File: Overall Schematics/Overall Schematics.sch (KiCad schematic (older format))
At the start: 31 parts, among them J1 WattMeter1_Output, J2 WattMeter2_Output, J3 Intel_Buck_Converter_Input, J4 WattMeter1_Input, J5 WattMeter2_Input, M1 Stepper_Motor_bipolar, M10 Motor_Servo, M11 Stepper_Motor_bipolar, M2 Stepper_Motor_bipolar, M3 LinActuator12V, M4 LinActuator12V, M5 LinActuator12V, M6 Motor_DC, M7 Motor_DC, M8 Motor_DC, M9 Motor_DC, SW1 SW_DPST, U1 Teensy4.1, U10 VNH52019, U11 ServoDriver, U12 36v4SMD, U2 36v4SMD, U3 36v4SMD, U4 VNH52019, U5 VNH52019, U6 VNH52019, U7 VNH52019, U8 VNH52019, U9 VNH52019

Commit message: did some pcb stuff
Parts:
- added M12: Motor_Servo, TerminalBlock:TerminalBlock_bornier-3_P5.08mm, symbol Motor:Motor_Servo
- BT1, BT2: footprint Custom Footprints:AMASS_XT60-F_1x02_P7.20mm_Vertical -> (none)
- J4, J5: footprint TerminalBlock:TerminalBlock_bornier-2_P5.08mm -> (none)
- SW1: footprint Button_Switch_SMD:SW_MEC_5GSH9 -> (none)
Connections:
- net Battery1_Positive24V: no longer J2.2 (Pin_2), U12.17 (VIN), U12.18 (VIN2), U2.17 (VIN), U2.18 (VIN2), U5.14 (VIN(5.5V-24V)), U7.14 (VIN(5.5V-24V)), U8.14 (VIN(5.5V-24V))
- net GND: now also M10.3 (-), U11.13 (-_1), U11.14 (-_2), M12.3 (-)
- net SS_1: now reaches M10.1 (PWM), U11.1 (Signal_1)
- net SS_2: now reaches U11.2 (Signal_2)
- net SS_2: now also M12.1 (PWM)
- net +5V: now reaches M10.2 (+), U11.7 (+_1)
- net +5V: now also U11.8 (+_2), M12.2 (+)
- net Battery1_Positive renamed Battery2_Positive
- new net Battery2_Positive24V: J2.2 (Pin_2), U12.17 (VIN), U12.18 (VIN2), U2.17 (VIN), U2.18 (VIN2), U5.14 (VIN(5.5V-24V)), U7.14 (VIN(5.5V-24V)), U8.14 (VIN(5.5V-24V))
- no-connect marks 103 -> 100
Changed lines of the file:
@@
 F 0 "BT1" V 27455 13850 50  0000 C CNN
 F 1 "True_Spec_Battery1" V 27546 13850 50  0000 C CNN
-F 2 "Custom Footprints:AMASS_XT60-F_1x02_P7.20mm_Vertical" V 27700 13910 50  0001 C CNN
+F 2 "" V 27700 13910 50  0001 C CNN
 F 3 "~" V 27700 13910 50  0001 C CNN
 	1    27700 13850
@@
 F 0 "SW1" H 28700 14475 50  0000 C CNN
 F 1 "SW_DPST" H 28700 14384 50  0000 C CNN
-F 2 "Button_Switch_SMD:SW_MEC_5GSH9" H 28700 14150 50  0001 C CNN
+F 2 "" H 28700 14150 50  0001 C CNN
 F 3 "~" H 28700 14150 50  0001 C CNN
 	1    28700 14150
@@
 F 0 "BT2" V 27455 14250 50  0000 C CNN
 F 1 "True_Spec_Battery2" V 27546 14250 50  0000 C CNN
-F 2 "Custom Footprints:AMASS_XT60-F_1x02_P7.20mm_Vertical" V 27700 14310 50  0001 C CNN
+F 2 "" V 27700 14310 50  0001 C CNN
 F 3 "~" V 27700 14310 50  0001 C CNN
 	1    27700 14250
@@
 F 0 "J4" H 29530 13842 50  0000 L CNN
 F 1 "WattMeter1_Input" H 29530 13751 50  0000 L CNN
-F 2 "TerminalBlock:TerminalBlock_bornier-2_P5.08mm" H 29450 13850 50  0001 C CNN
+F 2 "" H 29450 13850 50  0001 C CNN
 F 3 "~" H 29450 13850 50  0001 C CNN
 	1    29450 13850
@@
 F 0 "J5" H 29530 14292 50  0000 L CNN
 F 1 "WattMeter2_Input" H 29530 14201 50  0000 L CNN
-F 2 "TerminalBlock:TerminalBlock_bornier-2_P5.08mm" H 29450 14300 50  0001 C CNN
+F 2 "" H 29450 14300 50  0001 C CNN
 F 3 "~" H 29450 14300 50  0001 C CNN
 	1    29450 14300
@@
 Wire Wire Line
 	29050 13850 29250 13850
-Wire Wire Line
-	28900 14250 29100 14250
 Wire Wire Line
 	29100 14250 29100 14300
@@
 Wire Wire Line
 	27500 14250 27100 14250
-$Comp
-L Connector:Screw_Terminal_01x02 J3
-U 1 1 5FB615C9
-P 29150 14800
-F 0 "J3" H 29230 14792 50  0000 L CNN
-F 1 "Intel_Buck_Converter_Input" H 29230 14701 50  0000 L CNN
-F 2 "TerminalBlock:TerminalBlock_bornier-2_P5.08mm" H 29150 14800 50  0001 C CNN
-F 3 "~" H 29150 14800 50  0001 C CNN
-	1    29150 14800
-	1    0    0    -1
-$EndComp
 Text GLabel 27400 14800 2    20   Input ~ 0
 Battery1_Positive24V
 Text GLabel 27400 15250 2    20   Input ~ 0
 Battery2_Positive24V
-Wire Wire Line
-	28950 14800 28950 14700
-Wire Wire Line
-	28950 14700 28850 14700
-Wire Wire Line
-	28850 14700 28850 14750
-Wire Wire Line
-	28850 14750 28750 14750
-Wire Wire Line
-	28850 14700 28850 14650
-Wire Wire Line
-	28850 14650 28750 14650
-Connection ~ 28850 14700
-Text GLabel 28750 14650 0    39   Input ~ 0
-Battery1_Positive
 Text GLabel 28750 14750 0    39   Input ~ 0
 Battery2_Positive
@@
 Text GLabel 23700 16750 2    39   Input ~ 0
 Battery2_Positive24V
-Text GLabel 23700 15400 2    39   Input ~ 0
-Battery2_Positive24V
 Wire Wire Line
 	23600 15400 23600 15500
 Wire Wire Line
 	23600 15500 23700 15500
-Connection ~ 23600 15400
-Wire Wire Line
-	23600 15400 23700 15400
 Wire Notes Line
 	21750 13000 21750 17300
@@
 STEP_3
 $Comp
+L Motor:Motor_Servo M10
+U 1 1 601479AE
+P 20450 10700
+F 0 "M10" H 20782 10765 50  0000 L CNN
+F 1 "Motor_Servo" H 20782 10674 50  0000 L CNN
+F 2 "TerminalBlock:TerminalBlock_bornier-3_P5.08mm" H 20450 10510 50  0001 C CNN
+F 3 "http://forums.parallax.com/uploads/attachments/46831/74481.png" H 20450 10510 50  0001 C CNN
+	1    20450 10700
+	1    0    0    -1
+$EndComp
+Wire Wire Line
+	19800 10600 20150 10600
+Wire Wire Line
+	19650 11050 19650 11100
+Wire Wire Line
+	19650 11100 20050 11100
+Wire Wire Line
+	20050 11100 20050 10700
+Wire Wire Line
+	20050 10700 20150 10700
+Wire Wire Line
+	19150 10900 19100 10900
+Wire Wire Line
+	19100 10900 19100 11150
+Wire Wire Line
+	19100 11150 20100 11150
+Wire Wire Line
+	20100 11150 20100 10800
+Wire Wire Line
+	20100 10800 20150 10800
+NoConn ~ 19800 10700
+NoConn ~ 19800 10750
+NoConn ~ 19800 10800
+NoConn ~ 19800 10850
+NoConn ~ 19550 11050
+NoConn ~ 19500 11050
+NoConn ~ 19450 11050
+NoConn ~ 19400 11050
+NoConn ~ 19150 10800
+NoConn ~ 19150 10750
+NoConn ~ 19150 10700
+NoConn ~ 19150 10650
+Wire Notes Line
+	18900 10250 21300 10250
+NoConn ~ 18750 12700
+NoConn ~ 18750 12800
+Wire Wire Line
+	28900 14250 29100 14250
+$Comp
+L Connector:Screw_Terminal_01x02 J3
+U 1 1 5FB615C9
+P 29150 14800
+F 0 "J3" H 29230 14792 50  0000 L CNN
+F 1 "Intel_Buck_Converter_Input" H 29230 14701 50  0000 L CNN
+F 2 "TerminalBlock:TerminalBlock_bornier-2_P5.08mm" H 29150 14800 50  0001 C CNN
+F 3 "~" H 29150 14800 50  0001 C CNN
+	1    29150 14800
+	1    0    0    -1
+$EndComp
+Wire Wire Line
+	28750 14750 28950 14750
+Wire Wire Line
+	28950 14750 28950 14800
+Wire Notes Line
+	21300 11600 18900 11600
+Wire Notes Line
+	18900 10250 18900 11600
+Wire Notes Line
+	21300 10250 21300 11600
+$Comp
 L CustomLibrary:ServoDriver U11
 U 1 1 6010875A
@@
 $EndComp
 $Comp
-L Motor:Motor_Servo M10
-U 1 1 601479AE
-P 20450 10700
-F 0 "M10" H 20782 10765 50  0000 L CNN
-F 1 "Motor_Servo" H 20782 10674 50  0000 L CNN
-F 2 "TerminalBlock:TerminalBlock_bornier-3_P5.08mm" H 20450 10510 50  0001 C CNN
-F 3 "http://forums.parallax.com/uploads/attachments/46831/74481.png" H 20450 10510 50  0001 C CNN
-	1    20450 10700
-	1    0    0    -1
-$EndComp
-Wire Wire Line
-	19800 10600 20150 10600
-Wire Wire Line
-	19650 11050 19650 11100
-Wire Wire Line
-	19650 11100 20050 11100
-Wire Wire Line
-	20050 11100 20050 10700
-Wire Wire Line
-	20050 10700 20150 10700
-Wire Wire Line
-	19150 10900 19100 10900
-Wire Wire Line
-	19100 10900 19100 11150
-Wire Wire Line
-	19100 11150 20100 11150
-Wire Wire Line
-	20100 11150 20100 10800
-Wire Wire Line
-	20100 10800 20150 10800
-NoConn ~ 19800 10650
-NoConn ~ 19800 10700
-NoConn ~ 19800 10750
-NoConn ~ 19800 10800
-NoConn ~ 19800 10850
-NoConn ~ 19600 11050
-NoConn ~ 19550 11050
-NoConn ~ 19500 11050
-NoConn ~ 19450 11050
-NoConn ~ 19400 11050
-NoConn ~ 19150 10850
-NoConn ~ 19150 10800
-NoConn ~ 19150 10750
-NoConn ~ 19150 10700
-NoConn ~ 19150 10650
-Wire Notes Line
-	18900 10250 21300 10250
-Wire Notes Line
-	21300 10250 21300 11250
-Wire Notes Line
-	21300 11250 18900 11250
-Wire Notes Line
-	18900 11250 18900 10250
-NoConn ~ 18750 12700
-NoConn ~ 18750 12800
+L Motor:Motor_Servo M12
+U 1 1 6020790C
+P 20450 11350
+F 0 "M12" H 20782 11415 50  0000 L CNN
+F 1 "Motor_Servo" H 20782 11324 50  0000 L CNN
+F 2 "TerminalBlock:TerminalBlock_bornier-3_P5.08mm" H 20450 11160 50  0001 C CNN
+F 3 "http://forums.parallax.com/uploads/attachments/46831/74481.png" H 20450 11160 50  0001 C CNN
+	1    20450 11350
+	1    0    0    -1
+$EndComp
+Wire Wire Line
+	20150 11250 19950 11250
+Wire Wire Line
+	19950 11250 19950 10650
+Wire Wire Line
+	19150 10850 19000 10850
+Wire Wire Line
+	18950 10850 18950 11450
+Wire Wire Line
+	18950 11450 20150 11450
+Wire Wire Line
+	19600 11050 19600 11350
+Wire Wire Line
+	19600 11350 20150 11350
+Wire Wire Line
+	19600 11050 19650 11050
+Connection ~ 19600 11050
+Connection ~ 19650 11050
+Wire Wire Line
+	19150 10900 19150 10850
+Connection ~ 19150 10900
+Connection ~ 19150 10850
+$Comp
+L power:GND #PWR01
+U 1 1 602354FF
+P 19000 10600
+F 0 "#PWR01" H 19000 10350 50  0001 C CNN
+F 1 "GND" V 19005 10472 50  0000 R CNN
+F 2 "" H 19000 10600 50  0001 C CNN
+F 3 "" H 19000 10600 50  0001 C CNN
+	1    19000 10600
+	-1   0    0    1
+$EndComp
+Wire Wire Line
+	19000 10600 19000 10850
+Connection ~ 19000 10850
+Wire Wire Line
+	19000 10850 18950 10850
+Text GLabel 19900 10350 2    50   Input ~ 0
+SS_1
+Text GLabel 19900 10500 2    50   Input ~ 0
+SS_2
+Wire Wire Line
+	19800 10600 19800 10350
+Wire Wire Line
+	19800 10350 19900 10350
+Connection ~ 19800 10600
+Wire Wire Line
+	19900 10500 19900 10650
+Wire Wire Line
+	19800 10650 19900 10650
+Connection ~ 19900 10650
+Wire Wire Line
+	19900 10650 19950 10650
+$Comp
+L power:+5V #PWR?
+U 1 1 60266C9B
+P 19500 11350
+F 0 "#PWR?" H 19500 11200 50  0001 C CNN
+F 1 "+5V" V 19515 11478 50  0000 L CNN
+F 2 "" H 19500 11350 50  0001 C CNN
+F 3 "" H 19500 11350 50  0001 C CNN
+	1    19500 11350
+	0    -1   -1   0
+$EndComp
+Wire Wire Line
+	19500 11350 19600 11350
+Connection ~ 19600 11350
 $EndSCHEMATC

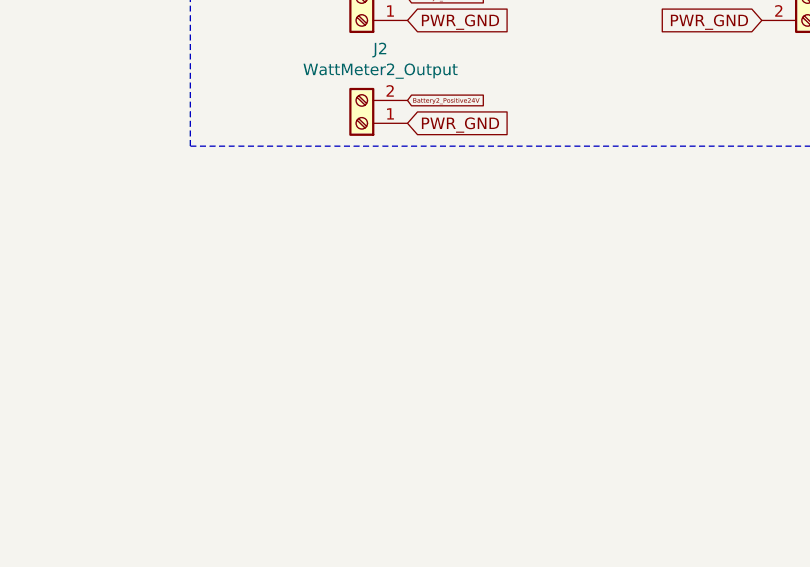
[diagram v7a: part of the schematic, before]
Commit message: Added 5V buck
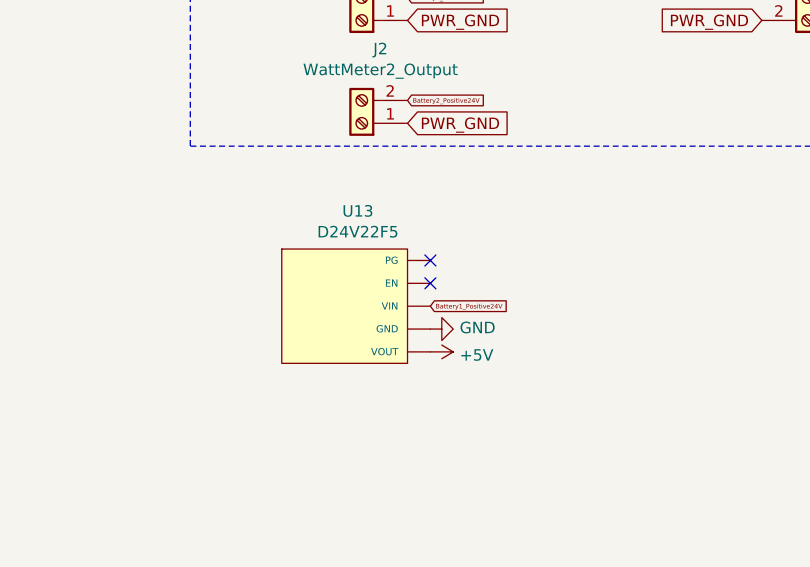
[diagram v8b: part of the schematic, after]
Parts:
- added U13: D24V22F5, Custom Footprints:D24V22F5, symbol CustomLibrary:D24V22F5
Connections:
- net +5V: now also U13.~ (VOUT)
- net Battery1_Positive24V: now also U13.~ (VOUT)
- net GND: now also U13.~ (VOUT)
- no-connect marks 100 -> 102
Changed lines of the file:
@@
 	19900 10650 19950 10650
 $Comp
-L power:+5V #PWR?
+L power:+5V #PWR02
 U 1 1 60266C9B
 P 19500 11350
-F 0 "#PWR?" H 19500 11200 50  0001 C CNN
+F 0 "#PWR02" H 19500 11200 50  0001 C CNN
 F 1 "+5V" V 19515 11478 50  0000 L CNN
 F 2 "" H 19500 11350 50  0001 C CNN
@@
 	19500 11350 19600 11350
 Connection ~ 19600 11350
+$Comp
+L CustomLibrary:D24V22F5 U13
+U 1 1 602879C7
+P 27150 15800
+F 0 "U13" H 27183 15865 50  0000 C CNN
+F 1 "D24V22F5" H 27183 15774 50  0000 C CNN
+F 2 "Custom Footprints:D24V22F5" H 27150 15800 50  0001 C CNN
+F 3 "" H 27150 15800 50  0001 C CNN
+	1    27150 15800
+	1    0    0    -1
+$EndComp
+NoConn ~ 27500 15950
+NoConn ~ 27500 16050
+$Comp
+L power:GND #PWR03
+U 1 1 6029495B
+P 27500 16250
+F 0 "#PWR03" H 27500 16000 50  0001 C CNN
+F 1 "GND" V 27505 16122 50  0000 R CNN
+F 2 "" H 27500 16250 50  0001 C CNN
+F 3 "" H 27500 16250 50  0001 C CNN
+	1    27500 16250
+	0    -1   -1   0
+$EndComp
+Text GLabel 27500 16150 2    20   Input ~ 0
+Battery1_Positive24V
+$Comp
+L power:+5V #PWR04
+U 1 1 602A1733
+P 27500 16350
+F 0 "#PWR04" H 27500 16200 50  0001 C CNN
+F 1 "+5V" V 27515 16478 50  0000 L CNN
+F 2 "" H 27500 16350 50  0001 C CNN
+F 3 "" H 27500 16350 50  0001 C CNN
+	1    27500 16350
+	0    1    1    0
+$EndComp
 $EndSCHEMATC
